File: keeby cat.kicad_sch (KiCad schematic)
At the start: 15 parts, among them SW12 SW_Push, SW14 SW_Push, SW15 SW_Push, SW3 SW_Push, SW6 SW_Push, SW9 SW_Push, U1 BluePill_V1.1

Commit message: routing improvements
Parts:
- added H5: MountingHole, Keeby-Cat Footprints:MountingHole_2.2mm_M2_DIN965, symbol Mechanical:MountingHole
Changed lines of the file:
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@@
+    )
+  )
+  (symbol (lib_id "Mechanical:MountingHole") (at 110.49 78.74 0) (unit 1)
+    (in_bom yes) (on_board yes) (fields_autoplaced)
+    (property "Reference" "H5" (id 0) (at 113.03 77.4699 0)
+      (effects (font (size 1.27 1.27)) (justify left))
+    )
+    (property "Value" "MountingHole" (id 1) (at 113.03 80.0099 0)
+      (effects (font (size 1.27 1.27)) (justify left))
+    )
+    (property "Footprint" "Keeby-Cat Footprints:MountingHole_2.2mm_M2_DIN965" (id 2) (at 110.49 78.74 0)
+      (effects (font (size 1.27 1.27)) hide)
+    )
+    (property "Datasheet" "~" (id 3) (at 110.49 78.74 0)
+      (effects (font (size 1.27 1.27)) hide)
     )
   )
@@
     )
     (path "/6ce8230c-595b-49b4-b7e1-27c56bb79809/3ce2fe9d-52b5-4ed5-906e-0b3e596089a9"
-      (reference "D4") (unit 1) (value "SK6812MINI-E") (footprint "Keeby-Cat Footprints:LED_MX_SK6812MINI-E")
+      (reference "D4") (unit 1) (value "SK6812MINI-E") (footprint "Keeby-Cat Footprints:LED_MX_SK6812MINI-E_rotated")
     )
     (path "/6ce8230c-595b-49b4-b7e1-27c56bb79809/5c324ce2-6999-456d-a7e3-26cd31e9fe5c"
-      (reference "D5") (unit 1) (value "SK6812MINI-E") (footprint "Keeby-Cat Footprints:LED_MX_SK6812MINI-E")
+      (reference "D5") (unit 1) (value "SK6812MINI-E") (footprint "Keeby-Cat Footprints:LED_MX_SK6812MINI-E_rotated")
     )
     (path "/6ce8230c-595b-49b4-b7e1-27c56bb79809/1225e9a7-7d2b-4330-acc2-96167debd483"
@@
     )
     (path "/6ce8230c-595b-49b4-b7e1-27c56bb79809/3b415046-c0f3-46bd-858f-63e0064bd46f"
-      (reference "D12") (unit 1) (value "SK6812MINI-E") (footprint "Keeby-Cat Footprints:LED_MX_SK6812MINI-E")
+      (reference "D12") (unit 1) (value "SK6812MINI-E") (footprint "Keeby-Cat Footprints:LED_MX_SK6812MINI-E_rotated")
     )
     (path "/6ce8230c-595b-49b4-b7e1-27c56bb79809/7eb787a0-452b-46a7-87c4-2964bd23114b"
@@
       (reference "H4") (unit 1) (value "MountingHole") (footprint "Keeby-Cat Footprints:MountingHole_2.2mm_M2_DIN965")
     )
+    (path "/eeee06f1-b1d6-4a0a-9afb-bc6f990265ed"
+      (reference "H5") (unit 1) (value "MountingHole") (footprint "Keeby-Cat Footprints:MountingHole_2.2mm_M2_DIN965")
+    )
     (path "/6ce8230c-595b-49b4-b7e1-27c56bb79809/368da0b2-4a09-4c1c-a7bd-9829d431f181"

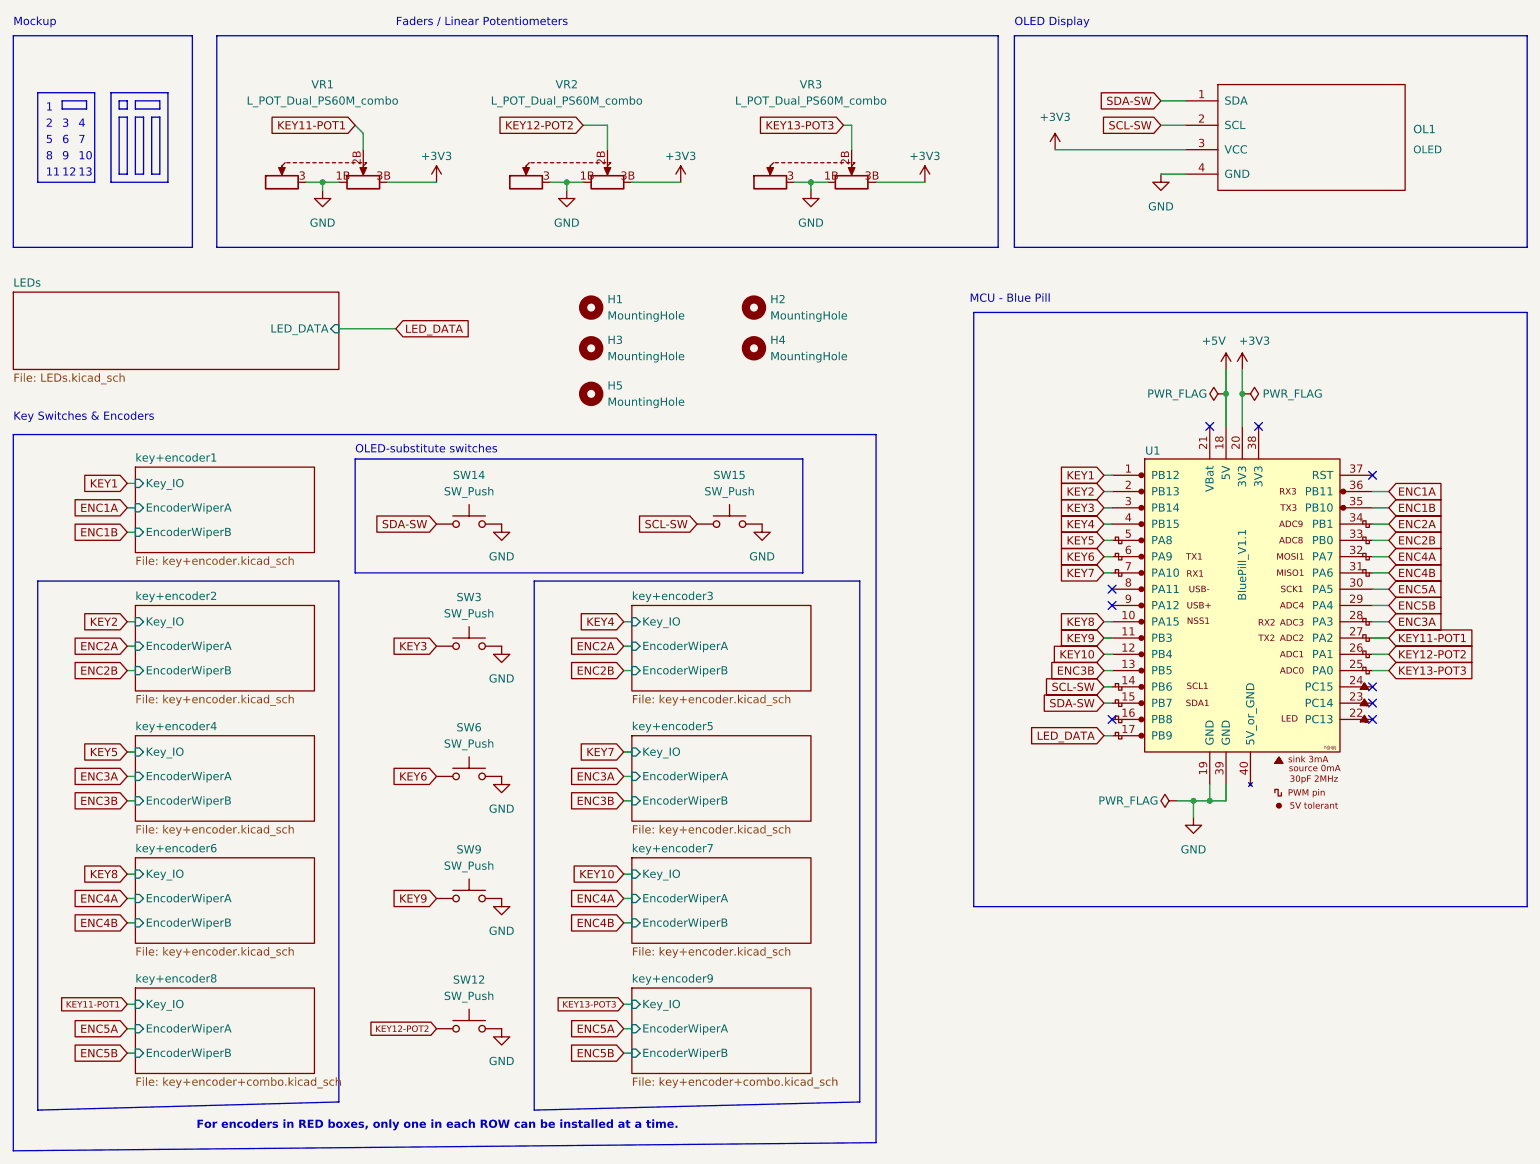
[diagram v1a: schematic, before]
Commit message: adjust schematic graphics
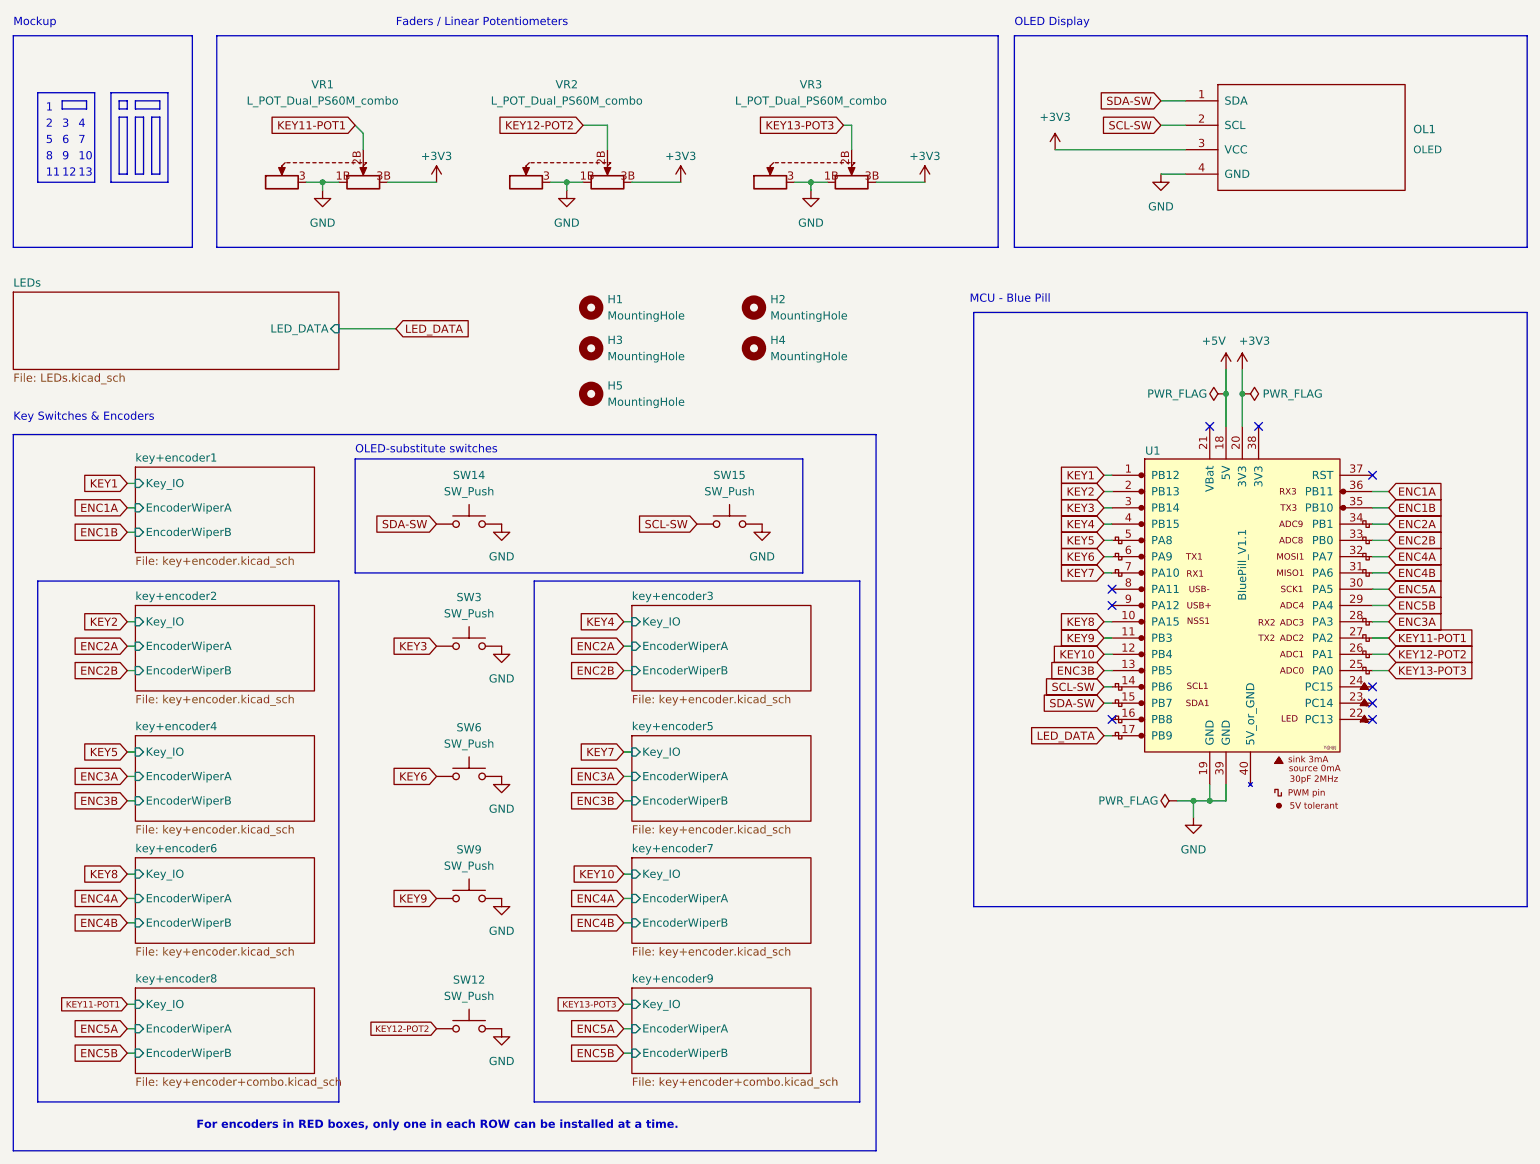
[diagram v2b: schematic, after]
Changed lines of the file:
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@@
     (stroke (width 0) (type default) (color 0 0 0 0))
   )
-  (polyline (pts (xy 24.13 190.5) (xy 71.12 189.23))
+  (polyline (pts (xy 24.13 189.23) (xy 71.12 189.23))
     (stroke (width 0) (type default) (color 194 0 0 1))
   )
@@
     (stroke (width 0) (type default) (color 0 0 0 0))
   )
-  (polyline (pts (xy 20.32 196.85) (xy 154.94 195.58))
-    (stroke (width 0) (type default) (color 0 0 0 0))
-  )
-  (polyline (pts (xy 154.94 195.58) (xy 154.94 85.09))
+  (polyline (pts (xy 20.32 196.85) (xy 154.94 196.85))
+    (stroke (width 0) (type default) (color 0 0 0 0))
+  )
+  (polyline (pts (xy 154.94 196.85) (xy 154.94 85.09))
     (stroke (width 0) (type default) (color 0 0 0 0))
   )
@@
     (stroke (width 0) (type default) (color 0 0 0 0))
   )
-  (polyline (pts (xy 101.6 107.95) (xy 101.6 190.5))
-    (stroke (width 0) (type default) (color 194 0 0 1))
-  )
-  (polyline (pts (xy 24.13 107.95) (xy 24.13 190.5))
+  (polyline (pts (xy 101.6 107.95) (xy 101.6 189.23))
+    (stroke (width 0) (type default) (color 194 0 0 1))
+  )
+  (polyline (pts (xy 24.13 107.95) (xy 24.13 189.23))
     (stroke (width 0) (type default) (color 194 0 0 1))
   )
@@
     (stroke (width 0) (type default) (color 0 0 0 0))
   )
-  (polyline (pts (xy 101.6 190.5) (xy 152.4 189.23))
-    (stroke (width 0) (type default) (color 194 0 0 1))
-  )
+  (polyline (pts (xy 101.6 189.23) (xy 152.4 189.23))
+    (stroke (width 0) (type default) (color 194 0 0 1))
+  )
